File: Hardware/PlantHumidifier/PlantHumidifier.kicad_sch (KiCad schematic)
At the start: 5 parts

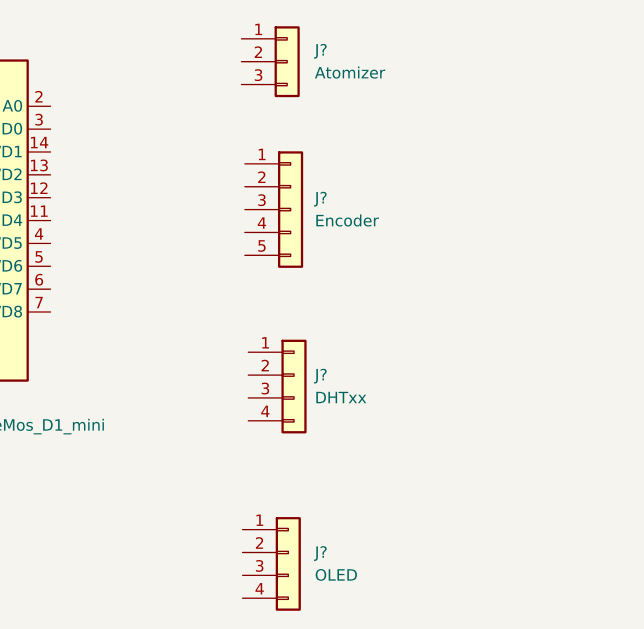
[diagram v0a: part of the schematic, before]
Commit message: Schematic: Layout connectors for all sensors
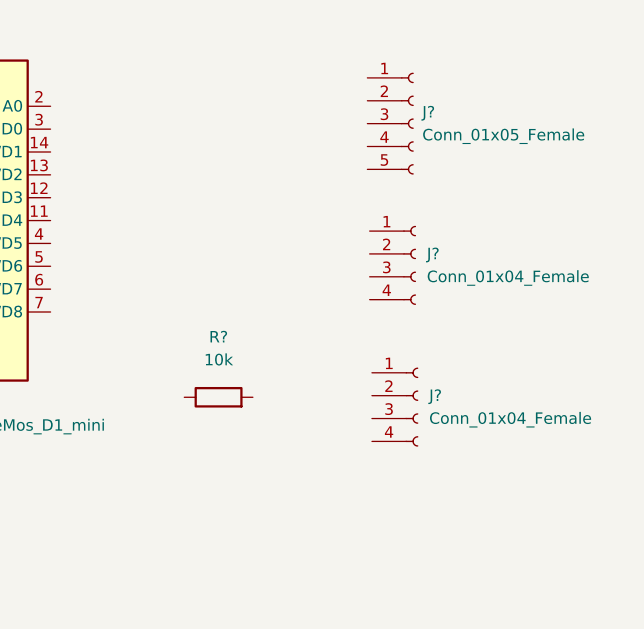
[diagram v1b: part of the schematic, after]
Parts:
- removed J?: Encoder, symbol Connector_Generic:Conn_01x05
- removed J?: Atomizer, symbol Connector_Generic:Conn_01x03
- removed J?: OLED, symbol Connector_Generic:Conn_01x04
- removed J?: DHTxx, symbol Connector_Generic:Conn_01x04
- added J? (x2): Conn_01x04_Female, symbol Connector:Conn_01x04_Female
- added J?: Conn_01x05_Female, symbol Connector:Conn_01x05_Female
- added R?: 10k, symbol Device:R
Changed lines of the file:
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@@
 (kicad_sch (version 20211123) (generator eeschema)
   (paper "A4")
-  (symbol (lib_id "Connector_Generic:Conn_01x05") (at 187.8076 106.8324 0) (unit 1)
+  (symbol (lib_id "Connector:Conn_01x04_Female") (at 201.676 111.76 0) (unit 1)
     (in_bom yes) (on_board yes) (fields_autoplaced)
-    (property "Reference" "J?" (id 0) (at 190.5 105.5623 0)
+    (property "Reference" "J?" (id 0) (at 202.946 111.7599 0)
       (effects (font (size 1.27 1.27)) (justify left))
     )
-    (property "Value" "Encoder" (id 1) (at 190.5 108.1023 0)
+    (property "Value" "Conn_01x04_Female" (id 1) (at 202.946 114.2999 0)
       (effects (font (size 1.27 1.27)) (justify left))
     )
-    (property "Footprint" "" (id 2) (at 187.8076 106.8324 0)
+    (property "Footprint" "" (id 2) (at 201.676 111.76 0)
       (effects (font (size 1.27 1.27)) hide)
     )
-    (property "Datasheet" "~" (id 3) (at 187.8076 106.8324 0)
+    (property "Datasheet" "~" (id 3) (at 201.676 111.76 0)
+      (effects (font (size 1.27 1.27)) hide)
+    )
+    (pin "1")
+    (pin "2")
+    (pin "3")
+    (pin "4")
+  )
+  (symbol (lib_id "Connector:Conn_01x04_Female") (at 201.93 127.508 0) (unit 1)
+    (in_bom yes) (on_board yes) (fields_autoplaced)
+    (property "Reference" "J?" (id 0) (at 203.2 127.5079 0)
+      (effects (font (size 1.27 1.27)) (justify left))
+    )
+    (property "Value" "Conn_01x04_Female" (id 1) (at 203.2 130.0479 0)
+      (effects (font (size 1.27 1.27)) (justify left))
+    )
+    (property "Footprint" "" (id 2) (at 201.93 127.508 0)
+      (effects (font (size 1.27 1.27)) hide)
+    )
+    (property "Datasheet" "~" (id 3) (at 201.93 127.508 0)
+      (effects (font (size 1.27 1.27)) hide)
+    )
+    (pin "1")
+    (pin "2")
+    (pin "3")
+    (pin "4")
+  )
+  (symbol (lib_id "Connector:Conn_01x05_Female") (at 201.422 97.282 0) (unit 1)
+    (in_bom yes) (on_board yes) (fields_autoplaced)
+    (property "Reference" "J?" (id 0) (at 202.438 96.0119 0)
+      (effects (font (size 1.27 1.27)) (justify left))
+    )
+    (property "Value" "Conn_01x05_Female" (id 1) (at 202.438 98.5519 0)
+      (effects (font (size 1.27 1.27)) (justify left))
+    )
+    (property "Footprint" "" (id 2) (at 201.422 97.282 0)
+      (effects (font (size 1.27 1.27)) hide)
+    )
+    (property "Datasheet" "~" (id 3) (at 201.422 97.282 0)
       (effects (font (size 1.27 1.27)) hide)
     )
@@
     (pin "5")
   )
-  (symbol (lib_id "Connector_Generic:Conn_01x03") (at 187.4266 90.3986 0) (unit 1)
+  (symbol (lib_id "Device:R") (at 179.8066 127.6858 90) (unit 1)
     (in_bom yes) (on_board yes) (fields_autoplaced)
-    (property "Reference" "J?" (id 0) (at 190.5 89.1285 0)
-      (effects (font (size 1.27 1.27)) (justify left))
-    )
-    (property "Value" "Atomizer" (id 1) (at 190.5 91.6685 0)
-      (effects (font (size 1.27 1.27)) (justify left))
-    )
-    (property "Footprint" "" (id 2) (at 187.4266 90.3986 0)
+    (property "Reference" "R?" (id 0) (at 179.8066 121.0056 90))
+    (property "Value" "10k" (id 1) (at 179.8066 123.5456 90))
+    (property "Footprint" "" (id 2) (at 179.8066 129.4638 90)
       (effects (font (size 1.27 1.27)) hide)
     )
-    (property "Datasheet" "~" (id 3) (at 187.4266 90.3986 0)
+    (property "Datasheet" "~" (id 3) (at 179.8066 127.6858 0)
       (effects (font (size 1.27 1.27)) hide)
     )
     (pin "1")
     (pin "2")
-    (pin "3")
-  )
-  (symbol (lib_id "Connector_Generic:Conn_01x04") (at 187.5536 144.9324 0) (unit 1)
-    (in_bom yes) (on_board yes) (fields_autoplaced)
-    (property "Reference" "J?" (id 0) (at 190.5 144.9323 0)
-      (effects (font (size 1.27 1.27)) (justify left))
-    )
-    (property "Value" "OLED" (id 1) (at 190.5 147.4723 0)
-      (effects (font (size 1.27 1.27)) (justify left))
-    )
-    (property "Footprint" "" (id 2) (at 187.5536 144.9324 0)
-      (effects (font (size 1.27 1.27)) hide)
-    )
-    (property "Datasheet" "~" (id 3) (at 187.5536 144.9324 0)
-      (effects (font (size 1.27 1.27)) hide)
-    )
-    (pin "1")
-    (pin "2")
-    (pin "3")
-    (pin "4")
-  )
-  (symbol (lib_id "Connector_Generic:Conn_01x04") (at 188.1886 125.222 0) (unit 1)
-    (in_bom yes) (on_board yes) (fields_autoplaced)
-    (property "Reference" "J?" (id 0) (at 190.5 125.2219 0)
-      (effects (font (size 1.27 1.27)) (justify left))
-    )
-    (property "Value" "DHTxx" (id 1) (at 190.5 127.7619 0)
-      (effects (font (size 1.27 1.27)) (justify left))
-    )
-    (property "Footprint" "" (id 2) (at 188.1886 125.222 0)
-      (effects (font (size 1.27 1.27)) hide)
-    )
-    (property "Datasheet" "~" (id 3) (at 188.1886 125.222 0)
-      (effects (font (size 1.27 1.27)) hide)
-    )
-    (pin "1")
-    (pin "2")
-    (pin "3")
-    (pin "4")
   )
   (symbol (lib_id "MCU_Module:WeMos_D1_mini") (at 150.9776 108.0516 0) (unit 1)
@@
   )
   (symbol_instances
-    (path "/0f456664-e4f9-4683-b085-477bb872eaf0"
-      (reference "J?") (unit 1) (value "Encoder") (footprint "")
+    (path "/83845b8d-1c62-4450-bceb-8208d6b21664"
+      (reference "J?") (unit 1) (value "Conn_01x04_Female") (footprint "")
     )
-    (path "/41a47ecf-1142-4024-b50b-c07e7bd8cbd6"
-      (reference "J?") (unit 1) (value "Atomizer") (footprint "")
+    (path "/9d350f87-3249-4139-b96d-540780875faa"
+      (reference "J?") (unit 1) (value "Conn_01x04_Female") (footprint "")
     )
-    (path "/9de5fe92-d647-47b9-9484-a140938f02cb"
-      (reference "J?") (unit 1) (value "OLED") (footprint "")
+    (path "/b462574f-43c5-4a1a-9527-fc39d017b1e6"
+      (reference "J?") (unit 1) (value "Conn_01x05_Female") (footprint "")
     )
-    (path "/b215804f-c555-4a55-b7c4-c785570fb43b"
-      (reference "J?") (unit 1) (value "DHTxx") (footprint "")
+    (path "/f889db46-da6a-4204-801e-ce755109cdb4"
+      (reference "R?") (unit 1) (value "10k") (footprint "")
     )
     (path "/fb8daade-f4cb-4b21-85db-6e6f772ccb5f"

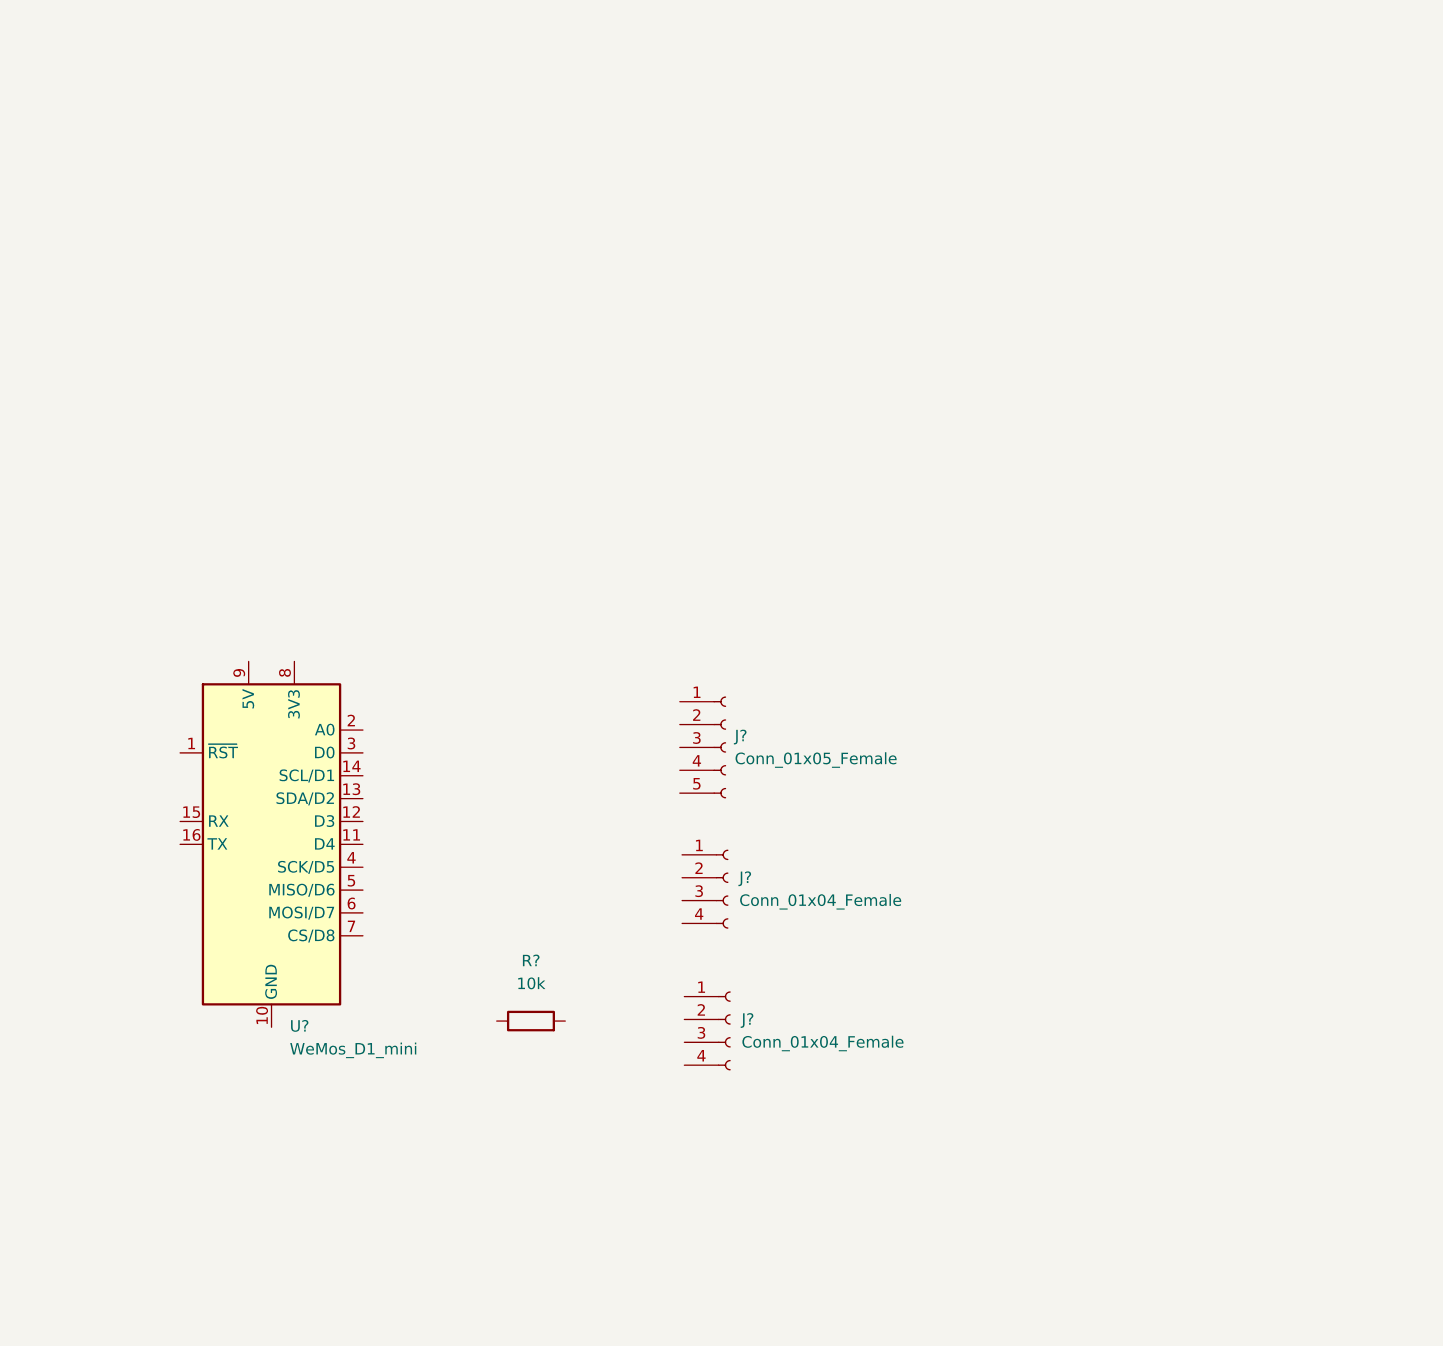
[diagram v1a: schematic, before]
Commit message: Schematic: Add filtering caps and wire DHT22
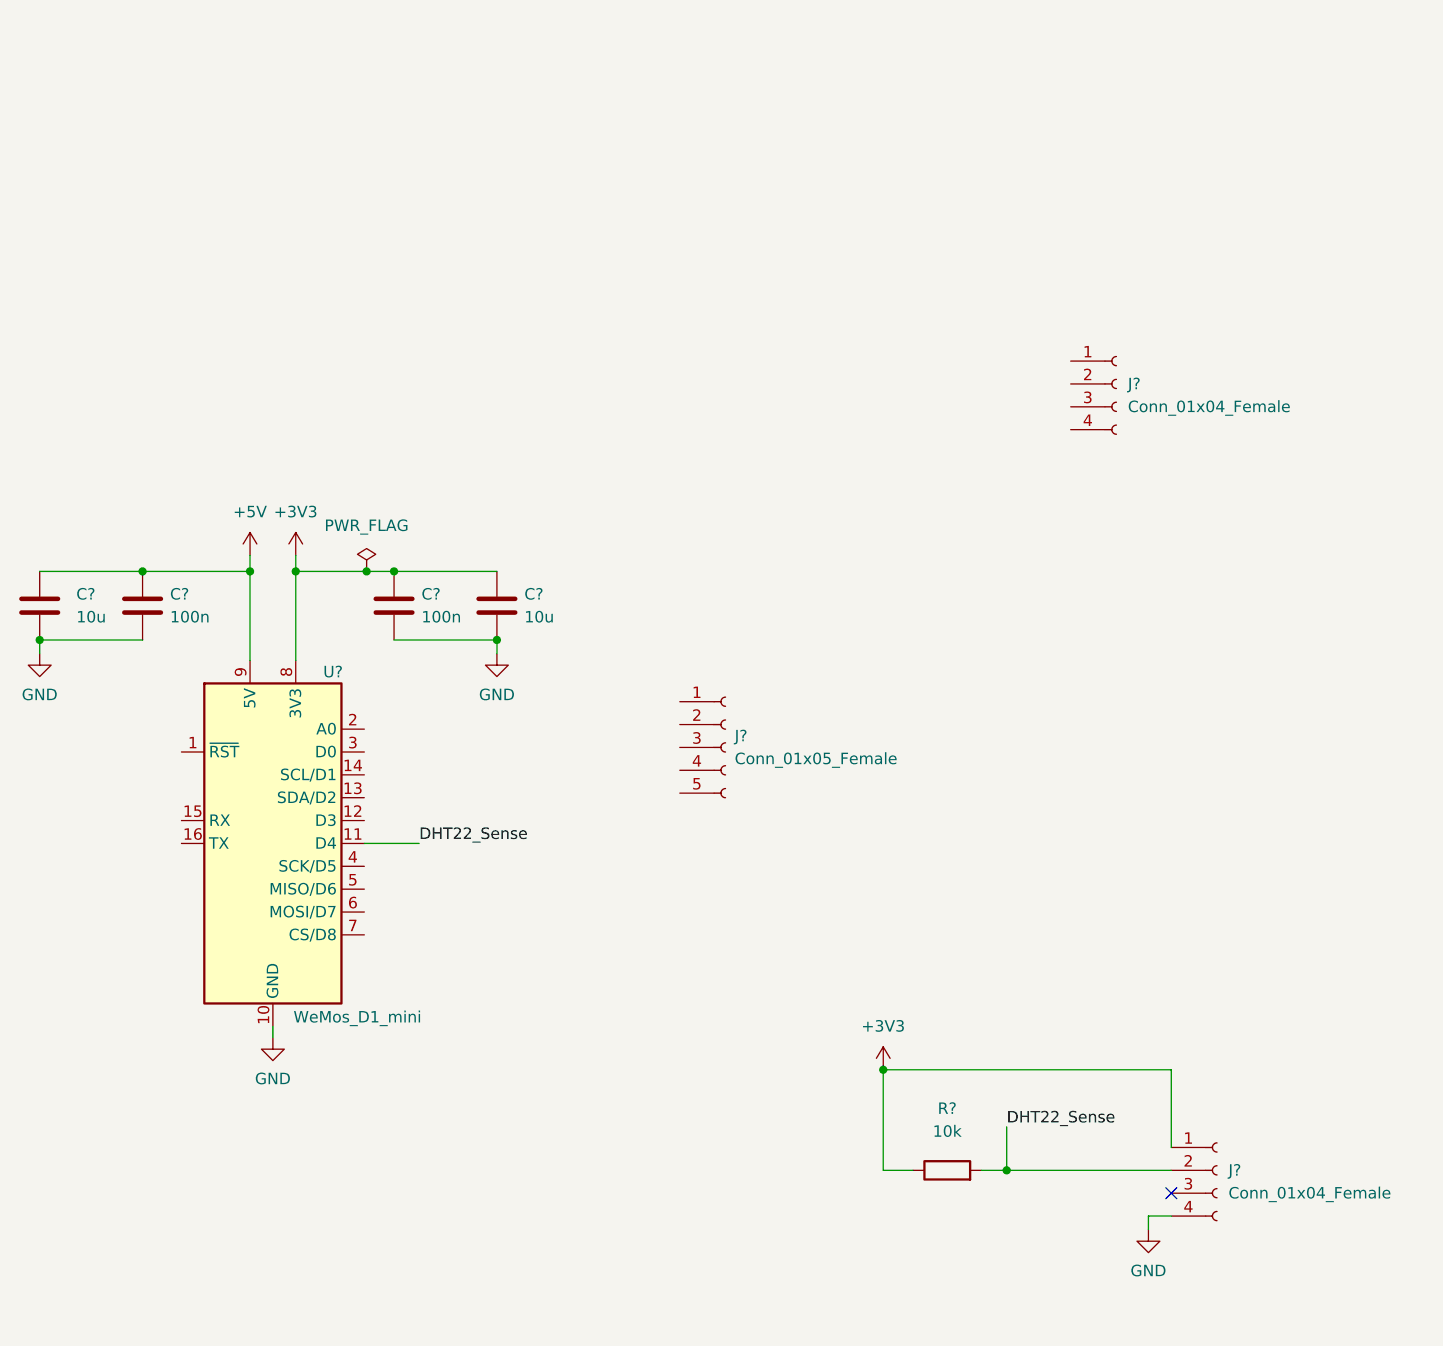
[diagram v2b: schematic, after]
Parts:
- removed R?: 10k, symbol Device:R
- added C? (x2): 100n, symbol Device:C
- added C? (x2): 10u, symbol Device:C
- added R?: 10k, symbol Device:R
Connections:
- net +3V3: now reaches J?.1 (Pin_1)
- net +3V3: now also U?.8 (3V3), C?.1, C?.1, R?.1
- net DHT22_Sense: now reaches J?.2 (Pin_2)
- net DHT22_Sense: now also U?.11 (D4), R?.2
- net GND: now reaches J?.4 (Pin_4)
- net GND: now also U?.10 (GND), C?.2, C?.2, C?.2, C?.2
- net +5V: now reaches U?.9 (5V)
- net +5V: now also C?.1, C?.1
- no-connect marks 0 -> 1
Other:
- moved on the sheet: J?
